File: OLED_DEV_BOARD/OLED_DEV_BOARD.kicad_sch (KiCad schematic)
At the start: 32 parts, among them J1 Barrel_Jack, J2 Conn_02x10_Odd_Even, J3 AudioJack3_Ground, J4 Conn_02x20_Odd_Even, SW1 SW_DIP_x02, SW2 SW_MEC_5E, SW3 SW_MEC_5E, SW4 SW_MEC_5E, SW5 SW_MEC_5E, SW6 SW_MEC_5E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

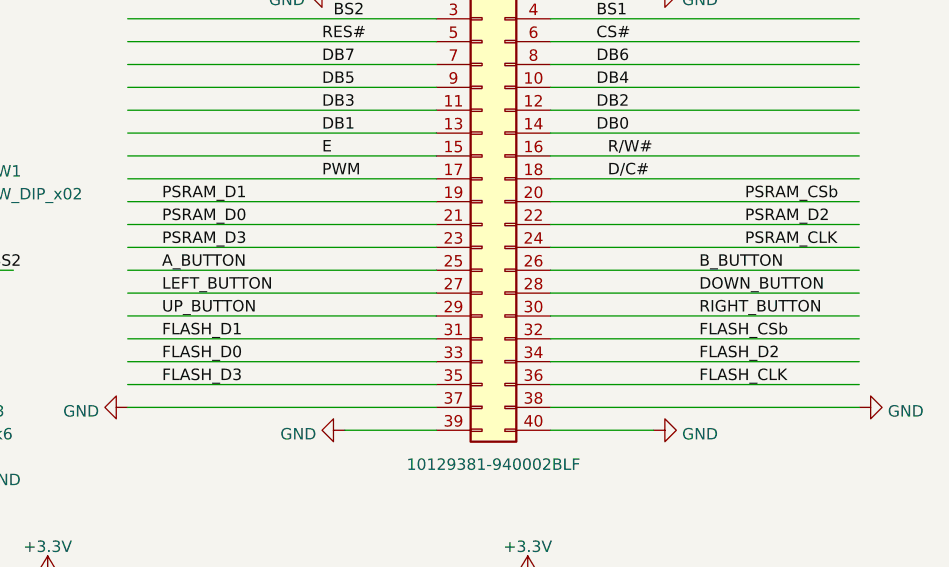
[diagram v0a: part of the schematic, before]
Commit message: Mostly routed
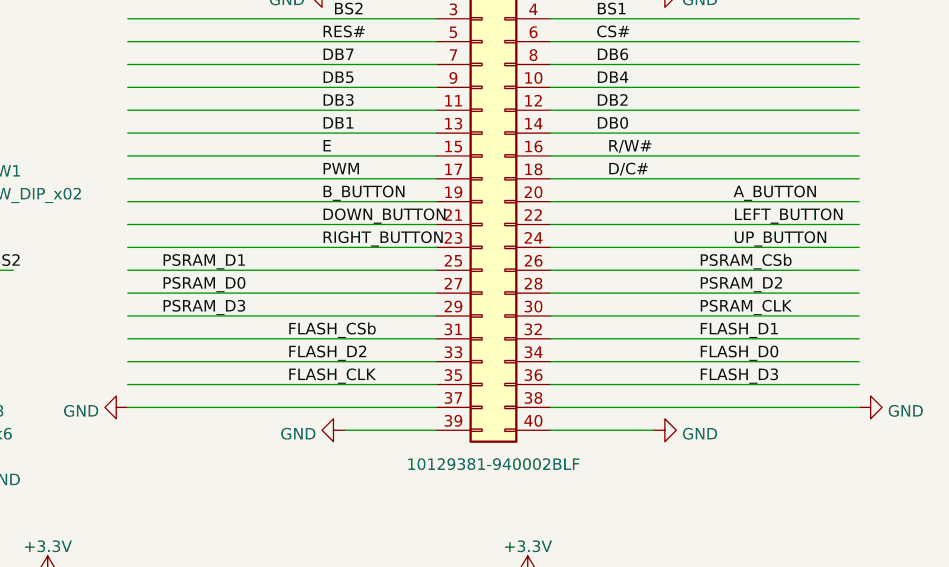
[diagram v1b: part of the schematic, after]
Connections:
- net A_BUTTON: now also J4.20 (Pin_20); no longer J4.25 (Pin_25)
- net B_BUTTON: now also J4.19 (Pin_19); no longer J4.26 (Pin_26)
- net DOWN_BUTTON: now also J4.21 (Pin_21); no longer J4.28 (Pin_28)
- net FLASH_CLK: now also J4.35 (Pin_35); no longer J4.36 (Pin_36)
- net FLASH_CSb: now also J4.31 (Pin_31); no longer J4.32 (Pin_32)
- net FLASH_D0: now also J4.34 (Pin_34); no longer J4.33 (Pin_33)
- net FLASH_D1: now also J4.32 (Pin_32); no longer J4.31 (Pin_31)
- net FLASH_D2: now also J4.33 (Pin_33); no longer J4.34 (Pin_34)
- net FLASH_D3: now also J4.36 (Pin_36); no longer J4.35 (Pin_35)
- net LEFT_BUTTON: now also J4.22 (Pin_22); no longer J4.27 (Pin_27)
- net PSRAM_CLK: now also J4.30 (Pin_30); no longer J4.24 (Pin_24)
- net PSRAM_CSb: now also J4.26 (Pin_26); no longer J4.20 (Pin_20)
- net PSRAM_D0: now also J4.27 (Pin_27); no longer J4.21 (Pin_21)
- net PSRAM_D1: now also J4.25 (Pin_25); no longer J4.19 (Pin_19)
- net PSRAM_D2: now also J4.28 (Pin_28); no longer J4.22 (Pin_22)
- net PSRAM_D3: now also J4.29 (Pin_29); no longer J4.23 (Pin_23)
- net RIGHT_BUTTON: now also J4.23 (Pin_23); no longer J4.30 (Pin_30)
- net UP_BUTTON: now also J4.24 (Pin_24); no longer J4.29 (Pin_29)
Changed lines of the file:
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@@
-    (effects (font (size 1.27 1.27)) (justify left bottom))
-  )
-  (label "UP_BUTTON" (at 163.83 73.66 0)
     (effects (font (size 1.27 1.27)) (justify left bottom))
   )
@@
     (effects (font (size 1.27 1.27)) (justify left bottom))
   )
-  (label "FLASH_D0" (at 163.83 78.74 0)
-    (effects (font (size 1.27 1.27)) (justify left bottom))
-  )
-  (label "PSRAM_CLK" (at 228.6 66.04 0)
-    (effects (font (size 1.27 1.27)) (justify left bottom))
-  )
-  (label "FLASH_D3" (at 163.83 81.28 0)
+  (label "FLASH_D1" (at 223.52 76.2 0)
     (effects (font (size 1.27 1.27)) (justify left bottom))
   )
@@
     (effects (font (size 1.27 1.27)) (justify left bottom))
   )
-  (label "PSRAM_D1" (at 163.83 60.96 0)
-    (effects (font (size 1.27 1.27)) (justify left bottom))
-  )
-  (label "A_BUTTON" (at 163.83 68.58 0)
+  (label "FLASH_D3" (at 223.52 81.28 0)
     (effects (font (size 1.27 1.27)) (justify left bottom))
   )
@@
     (effects (font (size 1.27 1.27)) (justify left bottom))
   )
-  (label "B_BUTTON" (at 223.52 68.58 0)
-    (effects (font (size 1.27 1.27)) (justify left bottom))
-  )
   (label "R{slash}W#" (at 213.36 55.88 0)
     (effects (font (size 1.27 1.27)) (justify left bottom))
   )
+  (label "PSRAM_D2" (at 223.52 71.12 0)
+    (effects (font (size 1.27 1.27)) (justify left bottom))
+  )
   (label "RIGHT_BUTTON" (at 215.9 134.62 0)
     (effects (font (size 1.27 1.27)) (justify left bottom))
   )
-  (label "PSRAM_D2" (at 228.6 63.5 0)
+  (label "PSRAM_D3" (at 163.83 73.66 0)
+    (effects (font (size 1.27 1.27)) (justify left bottom))
+  )
+  (label "PSRAM_D0" (at 163.83 71.12 0)
     (effects (font (size 1.27 1.27)) (justify left bottom))
   )
@@
     (effects (font (size 1.27 1.27)) (justify left bottom))
   )
-  (label "PSRAM_D0" (at 163.83 63.5 0)
-    (effects (font (size 1.27 1.27)) (justify left bottom))
-  )
-  (label "RIGHT_BUTTON" (at 223.52 73.66 0)
+  (label "B_BUTTON" (at 181.61 60.96 0)
+    (effects (font (size 1.27 1.27)) (justify left bottom))
+  )
+  (label "PSRAM_CLK" (at 223.52 73.66 0)
     (effects (font (size 1.27 1.27)) (justify left bottom))
   )
@@
     (effects (font (size 1.27 1.27)) (justify left bottom))
   )
+  (label "A_BUTTON" (at 227.33 60.96 0)
+    (effects (font (size 1.27 1.27)) (justify left bottom))
+  )
   (label "BS1" (at 128.27 66.04 0)
     (effects (font (size 1.27 1.27)) (justify left bottom))
   )
-  (label "FLASH_CLK" (at 223.52 81.28 0)
+  (label "UP_BUTTON" (at 227.33 66.04 0)
     (effects (font (size 1.27 1.27)) (justify left bottom))
   )
@@
     (effects (font (size 1.27 1.27)) (justify left bottom))
   )
-  (label "DOWN_BUTTON" (at 223.52 71.12 0)
-    (effects (font (size 1.27 1.27)) (justify left bottom))
-  )
   (label "DB7" (at 62.23 50.8 0)
     (effects (font (size 1.27 1.27)) (justify left bottom))
@@
     (effects (font (size 1.27 1.27)) (justify left bottom))
   )
-  (label "FLASH_D1" (at 163.83 76.2 0)
-    (effects (font (size 1.27 1.27)) (justify left bottom))
-  )
   (label "FLASH_CSb" (at 26.67 115.57 0)
     (effects (font (size 1.27 1.27)) (justify left bottom))
   )
-  (label "PSRAM_D3" (at 163.83 66.04 0)
-    (effects (font (size 1.27 1.27)) (justify left bottom))
-  )
   (label "E" (at 181.61 55.88 0)
     (effects (font (size 1.27 1.27)) (justify left bottom))
@@
     (effects (font (size 1.27 1.27)) (justify left bottom))
   )
+  (label "DOWN_BUTTON" (at 181.61 63.5 0)
+    (effects (font (size 1.27 1.27)) (justify left bottom))
+  )
   (label "D{slash}C#" (at 213.36 58.42 0)
     (effects (font (size 1.27 1.27)) (justify left bottom))
@@
     (effects (font (size 1.27 1.27)) (justify left bottom))
   )
+  (label "FLASH_CLK" (at 177.8 81.28 0)
+    (effects (font (size 1.27 1.27)) (justify left bottom))
+  )
   (label "A_BUTTON" (at 158.75 119.38 0)
     (effects (font (size 1.27 1.27)) (justify left bottom))
@@
     (effects (font (size 1.27 1.27)) (justify left bottom))
   )
+  (label "FLASH_D2" (at 177.8 78.74 0)
+    (effects (font (size 1.27 1.27)) (justify left bottom))
+  )
   (label "DB0" (at 29.21 43.18 0)
     (effects (font (size 1.27 1.27)) (justify left bottom))
@@
     (effects (font (size 1.27 1.27)) (justify left bottom))
   )
+  (label "PSRAM_D1" (at 163.83 68.58 0)
+    (effects (font (size 1.27 1.27)) (justify left bottom))
+  )
   (label "DB2" (at 212.09 50.8 0)
     (effects (font (size 1.27 1.27)) (justify left bottom))
@@
     (effects (font (size 1.27 1.27)) (justify left bottom))
   )
-  (label "FLASH_D2" (at 223.52 78.74 0)
+  (label "RIGHT_BUTTON" (at 181.61 66.04 0)
+    (effects (font (size 1.27 1.27)) (justify left bottom))
+  )
+  (label "PSRAM_CSb" (at 223.52 68.58 0)
+    (effects (font (size 1.27 1.27)) (justify left bottom))
+  )
+  (label "FLASH_D0" (at 223.52 78.74 0)
     (effects (font (size 1.27 1.27)) (justify left bottom))
   )
@@
     (effects (font (size 1.27 1.27)) (justify left bottom))
   )
+  (label "FLASH_CSb" (at 177.8 76.2 0)
+    (effects (font (size 1.27 1.27)) (justify left bottom))
+  )
   (label "DB6" (at 212.09 45.72 0)
     (effects (font (size 1.27 1.27)) (justify left bottom))
@@
     (effects (font (size 1.27 1.27)) (justify left bottom))
   )
-  (label "LEFT_BUTTON" (at 163.83 71.12 0)
-    (effects (font (size 1.27 1.27)) (justify left bottom))
-  )
-  (label "FLASH_CSb" (at 223.52 76.2 0)
-    (effects (font (size 1.27 1.27)) (justify left bottom))
-  )
   (label "BS2" (at 182.88 40.64 0)
     (effects (font (size 1.27 1.27)) (justify left bottom))
@@
     (effects (font (size 1.27 1.27)) (justify left bottom))
   )
-  (label "PSRAM_CSb" (at 228.6 60.96 0)
-    (effects (font (size 1.27 1.27)) (justify left bottom))
-  )
   (label "PSRAM_D1" (at 27.94 86.36 0)
     (effects (font (size 1.27 1.27)) (justify left bottom))
@@
     (effects (font (size 1.27 1.27)) (justify left bottom))
   )
+  (label "LEFT_BUTTON" (at 227.33 63.5 0)
+    (effects (font (size 1.27 1.27)) (justify left bottom))
+  )

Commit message: Added Fab Outputs
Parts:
- D1: footprint Diode_SMD:D_SMA -> Diode_THT:D_DO-41_SOD81_P10.16mm_Horizontal
- SW2, SW3, SW4, SW5, SW6, SW7: footprint Button_Switch_THT:SW_Tactile_Straight_KSA0Axx1LFTR -> OLED:SKHHAJA010
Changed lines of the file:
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@@
       (effects (font (size 1.27 1.27)) (justify right))
     )
-    (property "Footprint" "Button_Switch_THT:SW_Tactile_Straight_KSA0Axx1LFTR" (id 2) (at 147.32 143.51 0)
+    (property "Footprint" "OLED:SKHHAJA010" (id 2) (at 147.32 143.51 0)
       (effects (font (size 1.27 1.27)) hide)
     )
@@
     (property "Reference" "D1" (id 0) (at 90.17 128.3802 0))
     (property "Value" "FR1G" (id 1) (at 90.17 130.9171 0))
-    (property "Footprint" "Diode_SMD:D_SMA" (id 2) (at 90.17 137.795 0)
+    (property "Footprint" "Diode_THT:D_DO-41_SOD81_P10.16mm_Horizontal" (id 2) (at 90.17 137.795 0)
       (effects (font (size 1.27 1.27)) hide)
     )
@@
       (effects (font (size 1.27 1.27)) (justify right))
     )
-    (property "Footprint" "Button_Switch_THT:SW_Tactile_Straight_KSA0Axx1LFTR" (id 2) (at 224.79 128.27 0)
+    (property "Footprint" "OLED:SKHHAJA010" (id 2) (at 224.79 128.27 0)
       (effects (font (size 1.27 1.27)) hide)
     )
@@
       (effects (font (size 1.27 1.27)) (justify right))
     )
-    (property "Footprint" "Button_Switch_THT:SW_Tactile_Straight_KSA0Axx1LFTR" (id 2) (at 179.07 129.54 0)
+    (property "Footprint" "OLED:SKHHAJA010" (id 2) (at 179.07 129.54 0)
       (effects (font (size 1.27 1.27)) hide)
     )
@@
       (effects (font (size 1.27 1.27)) (justify right))
     )
-    (property "Footprint" "Button_Switch_THT:SW_Tactile_Straight_KSA0Axx1LFTR" (id 2) (at 199.39 111.76 0)
+    (property "Footprint" "OLED:SKHHAJA010" (id 2) (at 199.39 111.76 0)
       (effects (font (size 1.27 1.27)) hide)
     )
@@
       (effects (font (size 1.27 1.27)) (justify right))
     )
-    (property "Footprint" "Button_Switch_THT:SW_Tactile_Straight_KSA0Axx1LFTR" (id 2) (at 199.39 149.86 0)
+    (property "Footprint" "OLED:SKHHAJA010" (id 2) (at 199.39 149.86 0)
       (effects (font (size 1.27 1.27)) hide)
     )
@@
   )
   (symbol (lib_id "Regulator_Linear:NCP1117-3.3_TO252") (at 90.17 143.51 0) (unit 1)
-    (in_bom yes) (on_board yes) (fields_autoplaced)
+    (in_bom yes) (on_board yes)
     (property "Reference" "U3" (id 0) (at 90.17 137.9052 0))
     (property "Value" "NCP1117-3.3_TO252" (id 1) (at 90.17 140.4421 0))
@@
       (effects (font (size 1.27 1.27)) hide)
     )
-    (property "Manufacturer Part Number" "NCP1117DT33RKG" (id 4) (at 90.17 143.51 0)
-      (effects (font (size 1.27 1.27)) hide)
-    )
+    (property "Manufacturer Part Number" "NCP1117DT33RKG" (id 4) (at 88.9 157.48 0))
     (property "Mouser Part Number" "863-NCP1117DT33RKG" (id 5) (at 90.17 143.51 0)
       (effects (font (size 1.27 1.27)) hide)
@@
       (effects (font (size 1.27 1.27)) (justify right))
     )
-    (property "Footprint" "Button_Switch_THT:SW_Tactile_Straight_KSA0Axx1LFTR" (id 2) (at 146.05 111.76 0)
+    (property "Footprint" "OLED:SKHHAJA010" (id 2) (at 146.05 111.76 0)
       (effects (font (size 1.27 1.27)) hide)
     )
@@
     )
     (path "/18ac07ce-df99-4b15-b1c7-1a6f6425b01c"
-      (reference "D1") (unit 1) (value "FR1G") (footprint "Diode_SMD:D_SMA")
+      (reference "D1") (unit 1) (value "FR1G") (footprint "Diode_THT:D_DO-41_SOD81_P10.16mm_Horizontal")
     )
     (path "/aaf01c9a-c9a3-4e42-a983-ec360a40fbc7"
@@
     )
     (path "/ec794d10-bd06-4930-9be8-cffa5d6a2ec5"
-      (reference "SW2") (unit 1) (value "SW_MEC_5E") (footprint "Button_Switch_THT:SW_Tactile_Straight_KSA0Axx1LFTR")
+      (reference "SW2") (unit 1) (value "SW_MEC_5E") (footprint "OLED:SKHHAJA010")
     )
     (path "/01e98450-684e-414d-a12c-179b96fd374a"
-      (reference "SW3") (unit 1) (value "SW_MEC_5E") (footprint "Button_Switch_THT:SW_Tactile_Straight_KSA0Axx1LFTR")
+      (reference "SW3") (unit 1) (value "SW_MEC_5E") (footprint "OLED:SKHHAJA010")
     )
     (path "/45f61841-80c4-4af5-8bb0-7741db19f2f8"
-      (reference "SW4") (unit 1) (value "SW_MEC_5E") (footprint "Button_Switch_THT:SW_Tactile_Straight_KSA0Axx1LFTR")
+      (reference "SW4") (unit 1) (value "SW_MEC_5E") (footprint "OLED:SKHHAJA010")
     )
     (path "/6fb7e6ef-3c32-473b-89b1-c98aeacad6fb"
-      (reference "SW5") (unit 1) (value "SW_MEC_5E") (footprint "Button_Switch_THT:SW_Tactile_Straight_KSA0Axx1LFTR")
+      (reference "SW5") (unit 1) (value "SW_MEC_5E") (footprint "OLED:SKHHAJA010")
     )
     (path "/71dc5a86-fd4b-444d-a698-d75eb62cc7cc"
-      (reference "SW6") (unit 1) (value "SW_MEC_5E") (footprint "Button_Switch_THT:SW_Tactile_Straight_KSA0Axx1LFTR")
+      (reference "SW6") (unit 1) (value "SW_MEC_5E") (footprint "OLED:SKHHAJA010")
     )
     (path "/27a9bd5c-078b-492e-9cbc-8493131dfe5f"
-      (reference "SW7") (unit 1) (value "SW_MEC_5E") (footprint "Button_Switch_THT:SW_Tactile_Straight_KSA0Axx1LFTR")
+      (reference "SW7") (unit 1) (value "SW_MEC_5E") (footprint "OLED:SKHHAJA010")
     )
     (path "/bdde9e11-7801-483e-9088-385c57e7afa3"
